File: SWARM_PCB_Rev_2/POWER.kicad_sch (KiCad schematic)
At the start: 56 parts, among them J18 Conn_01x08_Pin, J2 XT30PW-M, U7 LMR33630ADDA, U8 LMR33630ADDA, U9 TPS55340RTER

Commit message: Reannotated Schematic
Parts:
- removed C33, C42: (no value), Capacitor_SMD:C_0603_1608Metric, symbol Device:C
- renumbered C56 to bC1, C37 to bC10, C55 to bC11, C31 to bC12, C41 to bC13, C38 to bC14, C39 to bC15, C43 to bC16, C44 to bC17, C45 to bC18, C46 to bC19, C57 to bC2, C40 to bC20, C47 to bC21, C50 to bC22, C51 to bC23, C49 to bC24, C48 to bC25, C32 to bC3, C30 to bC4, C29 to bC5, C54 to bC6, C34 to bC7, C35 to bC8, C36 to bC9, D8 to bD1, D4 to bD2, D5 to bD3, D6 to bD4, D7 to bD5, F1 to bF1, J2 to bJ1, J18 to bJ2, L1 to bL1, L2 to bL2, L3 to bL3, R24 to bR1, R33 to bR10, R34 to bR11, R32 to bR12, R35 to bR13, R30 to bR14, R31 to bR15, R21 to bR2, R22 to bR3, R23 to bR4, R25 to bR5, R26 to bR6, R28 to bR7, R29 to bR8, R27 to bR9, U7 to bU1, U8 to bU2, U9 to bU3

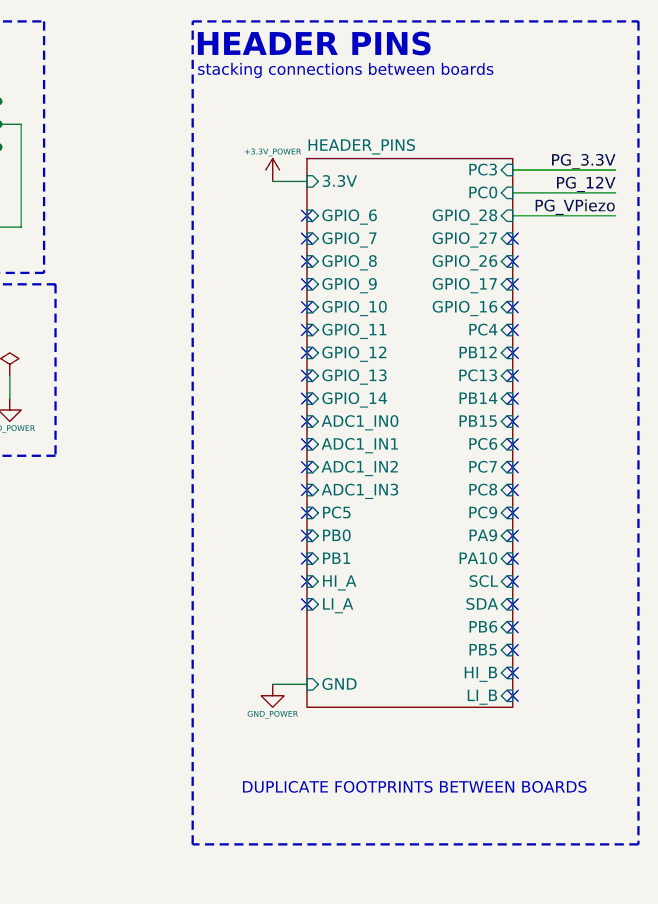
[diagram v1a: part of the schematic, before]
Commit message: Finished Placement for POWER, CONTROL and SENSOR
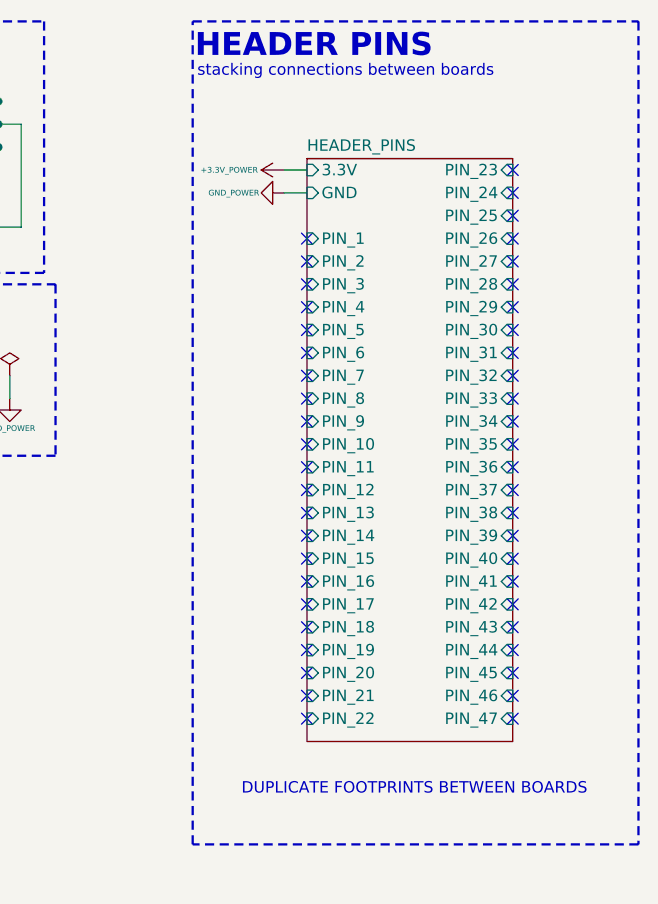
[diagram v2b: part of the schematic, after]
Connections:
- no-connect marks 41 -> 49
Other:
- sheet HEADER_PINS ports: added PIN_1, PIN_10, PIN_11, PIN_12, PIN_13, PIN_14, PIN_15, PIN_16, PIN_17, PIN_18, PIN_19, PIN_2, PIN_20, PIN_21, PIN_22, PIN_23, PIN_24, PIN_25, PIN_26, PIN_27, PIN_28, PIN_29, PIN_3, PIN_30, PIN_31, PIN_32, PIN_33, PIN_34, PIN_35, PIN_36, PIN_37, PIN_38, PIN_39, PIN_4, PIN_40, PIN_41, PIN_42, PIN_43, PIN_44, PIN_45, PIN_46, PIN_47, PIN_5, PIN_6, PIN_7, PIN_8, PIN_9; removed ADC1_IN0, ADC1_IN1, ADC1_IN2, ADC1_IN3, GPIO_10, GPIO_11, GPIO_12, GPIO_13, GPIO_14, GPIO_16, GPIO_17, GPIO_26, GPIO_27, GPIO_28, GPIO_6, GPIO_7, GPIO_8, GPIO_9, HI_A, HI_B, LI_A, LI_B, PA10, PA9, PB0, PB1, PB12, PB14, PB15, PB5, PB6, PC0, PC13, PC3, PC4, PC5, PC6, PC7, PC8, PC9, SCL, SDA

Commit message: Completed PCB Layout
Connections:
- net +12V_POWER: now also bJ2.2 (Pin_2), bJ2.3 (Pin_3); no longer bJ2.4 (Pin_4)
- net +VPiezo_POWER: now also bJ2.5 (Pin_5)
- net GND_POWER: now also bJ2.4 (Pin_4); no longer bJ2.3 (Pin_3), bJ2.5 (Pin_5)
- no-connect marks 49 -> 45
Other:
- note removed: "1.65V"
